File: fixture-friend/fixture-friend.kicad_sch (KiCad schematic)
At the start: 35 parts, among them J1 10103594-0001LF, J2 TSW-102-07-G-S, U1 NCP1117ST33T3G, U2 W25Q128JVSIQ, U3 RP2040, X1 12MHz

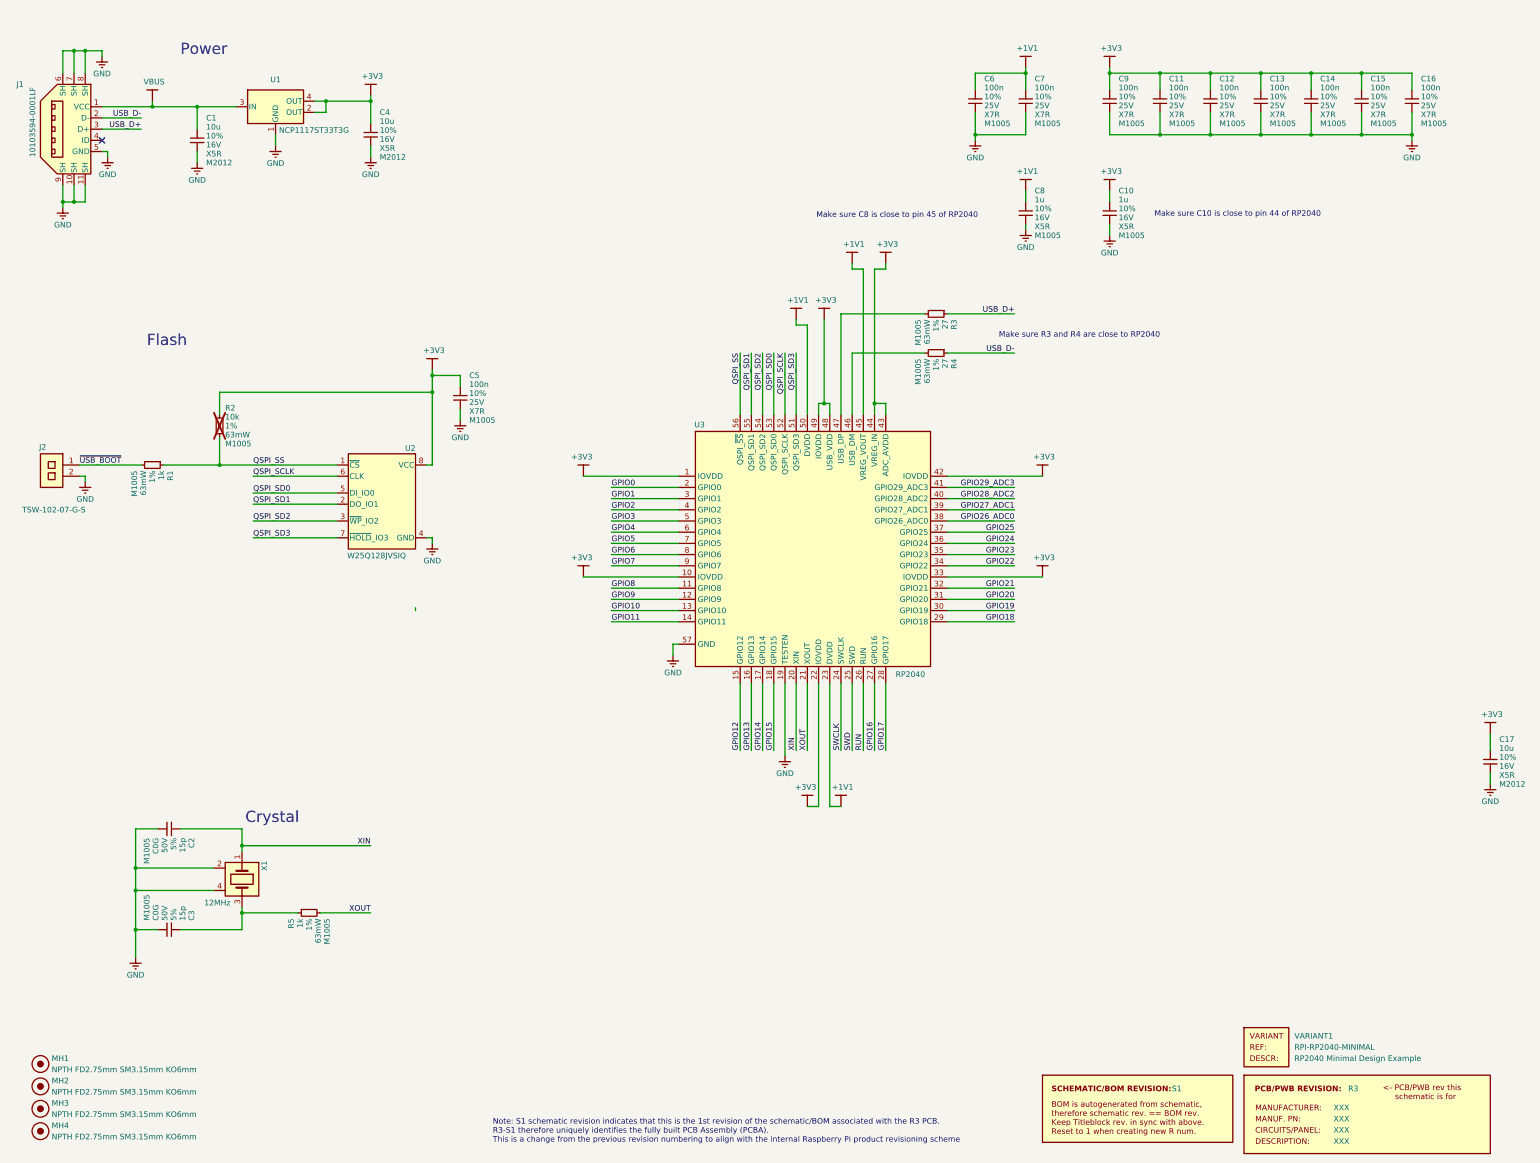
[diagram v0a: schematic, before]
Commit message: Added modular sub block for the SCH
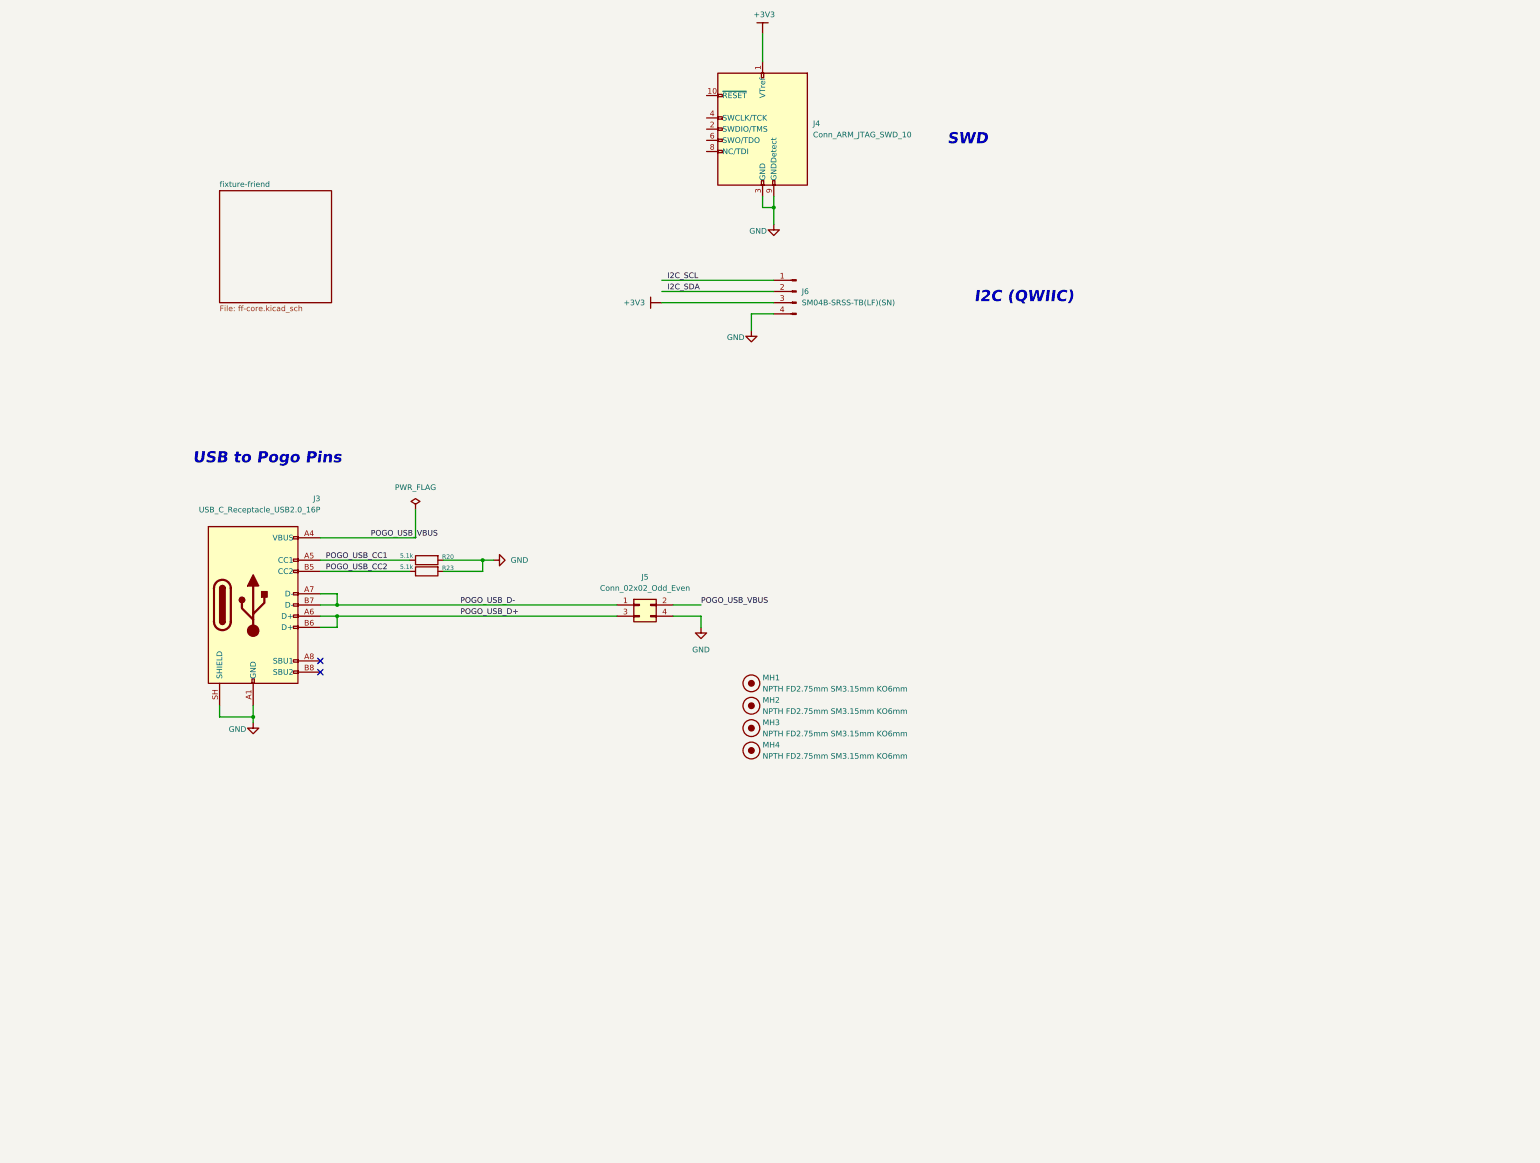
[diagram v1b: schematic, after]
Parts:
- removed C1, C17, C4: 10u, RPI_COMPILED:generic_capc2012x125, symbol RPI_DB:Capacitors | MLCC | M2012/RP-01GYSK-AVBE41
- removed C10, C8: 1u, RPI_COMPILED:generic_capc1005x50, symbol RPI_DB:Capacitors | MLCC | M1005/RP-01GYSK-L7FEKV
- removed C11, C12, C13, C14, C15, C16, C5, C6, C7, C9: 100n, RPI_COMPILED:generic_capc1005x50, symbol RPI_DB:Capacitors | MLCC | M1005/RP-01BJ9Y-KRGF41
- removed C2, C3: 15p, RPI_COMPILED:generic_capc1005x50, symbol RPI_DB:Capacitors | MLCC | M1005/RP-01C89W-LLY9XV
- removed J1: 10103594-0001LF, RPI_COMPILED:amphenol_10103594-0001lf, symbol RPI_DB:Connectors | USB/RP-019A1P-1JAX7V
- removed J2: TSW-102-07-G-S, RPI_COMPILED:samtec_tsw-102-07-g-s, symbol RPI_DB:Connectors | Pin_Headers/RP-01JV5X-LY21H5
- removed PCB1: R3, symbol RPI - BOM Directives:PCB_PWB_REV
- removed R1, R5: 1k, RPI_COMPILED:generic_resc1005x35, symbol RPI_DB:Resistors | Chip | M1005/RP-019A1P-4Z6ZWY
- removed R2: 10k, RPI_COMPILED:generic_resc1005x35, symbol RPI_DB:Resistors | Chip | M1005/RP-019A1P-53DHSX
- removed R3, R4: 27, RPI_COMPILED:generic_resc1005x35, symbol RPI_DB:Resistors | Chip | M1005/RP-01C89V-LTEYC4
- removed SBREV1: S1, symbol RPI - BOM Directives:SCH_BOM_REV
- removed U1: NCP1117ST33T3G, RPI_COMPILED:onsemi_ncp1117st33t3g, symbol RPI_DB:Integrated_Circuits | Power | LDO/RP-01JWD9-7JRX6J
- removed U2: W25Q128JVSIQ, RPI_COMPILED:generic_soic127p790x195-8, symbol RPI_DB:Integrated_Circuits | Memory | Serial_Flash | SPI/RP-01JWD4-F1H4N9
- removed U3: RP2040, RPI_COMPILED:rpi_rp2040_vias, symbol RPI_DB:Integrated_Circuits | Microcontrollers/RP-01EKHS-ZTKTEH
- removed VARIANT1: RPI-RP2040-MINIMAL, symbol RPI - BOM Directives:VARIANT
- removed X1: 12MHz, RPI_COMPILED:generic_xtalcc320x250x80-4, symbol RPI_DB:Frequency_Timing | Crystals/RP-01G8X7-GS352B
- added J3: USB_C_Receptacle_USB2.0_16P, Connector_USB:USB_C_Receptacle_GCT_USB4085, symbol Connector:USB_C_Receptacle_USB2.0_16P
- added J4: Conn_ARM_JTAG_SWD_10, symbol Connector:Conn_ARM_JTAG_SWD_10
- added J5: Conn_02x02_Odd_Even, Harwin_P70-2200045:Harwin_P70-2200045_2x02_P2.54mm, symbol Connector_Generic:Conn_02x02_Odd_Even
- added J6: SM04B-SRSS-TB(LF)(SN), Connector_JST:JST_SH_SM04B-SRSS-TB_1x04-1MP_P1.00mm_Horizontal, symbol Connector:Conn_01x04_Pin
- added R20, R23: 5.1k, Resistor_SMD:R_0603_1608Metric, symbol Device:R
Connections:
- net +3V3: now also J4.1 (VTref), J6.3 (Pin_3)
- net GND: now also J3.A1 (GND), J3.A12 (GND), J3.B1 (GND), J3.B12 (GND), J3.SH (SHIELD), J4.3 (GND), J4.5 (GND), J4.9 (GNDDetect), J5.4 (Pin_4), J6.4 (Pin_4), R20.2, R23.2
- new net I2C_SCL: J6.1 (Pin_1)
- new net I2C_SDA: J6.2 (Pin_2)
- new net POGO_USB_CC1: J3.A5 (CC1), R20.1
- new net POGO_USB_CC2: J3.B5 (CC2), R23.1
- new net POGO_USB_D+: J3.A6 (D+), J3.B6 (D+), J5.3 (Pin_3)
- new net POGO_USB_D-: J3.A7 (D-), J3.B7 (D-), J5.1 (Pin_1)
- new net POGO_USB_VBUS: J3.A4 (VBUS), J3.A9 (VBUS), J3.B4 (VBUS), J3.B9 (VBUS), J5.2 (Pin_2)
- no-connect marks 1 -> 2
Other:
- added sheet fixture-friend (ff-core.kicad_sch)
- note added: "I2C (QWIIC)"
- note added: "SWD"
- note added: "USB to Pogo Pins"
- note removed: "Crystal"
- note removed: "Flash"
- note removed: "Make sure C10 is close to pin 44 of RP2040"
- note removed: "Make sure C8 is close to pin 45 of RP2040"
- note removed: "Make sure R3 and R4 are close to RP2040"
- note removed: "Note: S1 schematic revision indicates that this is the 1st revision of the schematic/BOM associated with the R3 PCB. R3-S1 therefore uniquely identifies the fully built PCB Assembly (PCBA). This is a change from the previous revision numbering to align with the internal Raspberry Pi product revisioning scheme"
- note removed: "Power"
- moved on the sheet: MH1, MH2, MH3, MH4

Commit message: Add RP2040 debug interfaces
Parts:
- removed J4: Conn_ARM_JTAG_SWD_10, symbol Connector:Conn_ARM_JTAG_SWD_10
- added J1: Conn_ARM_JTAG_SWD_10, Connector_PinHeader_1.27mm:PinHeader_2x05_P1.27mm_Vertical_SMD, symbol Connector:Conn_ARM_JTAG_SWD_10
- added J8: 53261-0471, Connector_Molex:Molex_PicoBlade_53261-0471_1x04-1MP_P1.25mm_Horizontal, symbol Connector:Conn_01x04_Pin
- added J9: SM06B-SRSS-TB(LF)(SN), Connector_JST:JST_SH_SM06B-SRSS-TB_1x06-1MP_P1.00mm_Horizontal, symbol Connector:Conn_01x06_Pin
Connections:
- net +3V3: now also J1.1 (VTref), J8.2 (Pin_2), J9.2 (Pin_2)
- net GND: now also J1.3 (GND), J1.5 (GND), J1.9 (GNDDetect), J8.1 (Pin_1), J9.1 (Pin_1)
- new net PROBE_SWCLK: J1.4 (SWCLK/TCK)
- new net PROBE_SWDIO: J1.2 (SWDIO/TMS)
- new net SPI1_CS_N: J9.6 (Pin_6)
- new net SPI1_MISO: J9.5 (Pin_5)
- new net SPI1_MOSI: J9.4 (Pin_4)
- new net SPI1_SCK: J9.3 (Pin_3)
- new net UART1_RX: J8.4 (Pin_4)
- new net UART1_TX: J8.3 (Pin_3)
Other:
- sheet fixture-friend ports: added PROBE_SWCLK, PROBE_SWDIO, SPI1_CS_N, SPI1_MISO, SPI1_MOSI, SPI1_SCK, UART1_RX, UART1_TX; removed none
- note added: "SPI DEBUG (J9)"
- note added: "UART DEBUG (J8)"
